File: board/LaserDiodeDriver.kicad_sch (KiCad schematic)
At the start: 54 parts, among them K1 G5V-2_Split, Q1 2N7002, Q2 IRF9Z34, SW1 SW_SPDT, U1 LM317_TO-220, U2 OPA4192, U3 LT1009

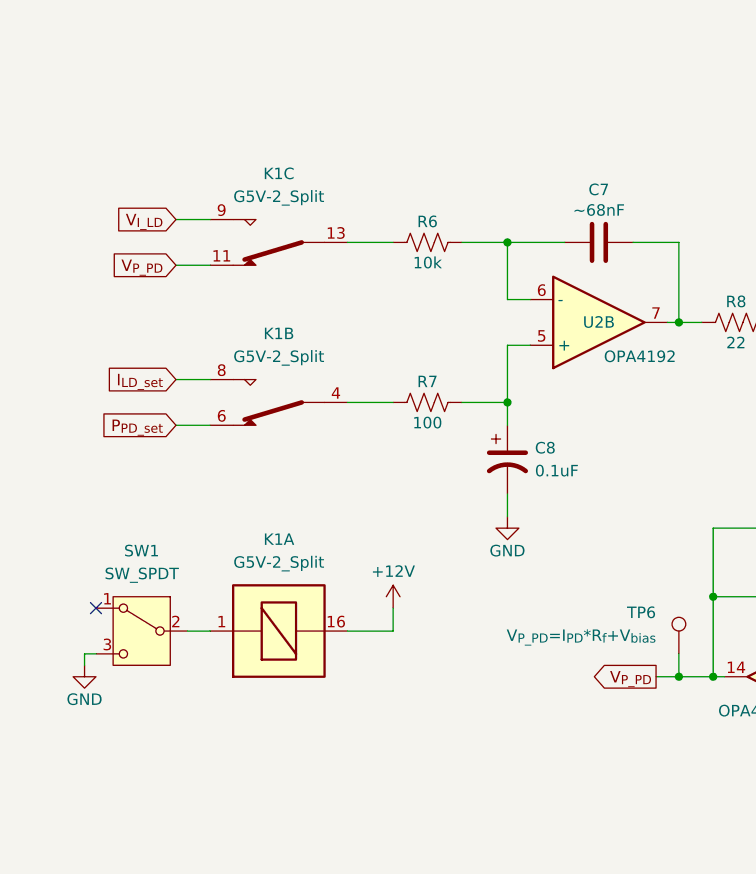
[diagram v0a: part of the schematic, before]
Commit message: Swapped to different signal relay
Since the signal relay is so large relative to all other components, It may be better to find an alternative. Something quicker than 0 Ohm jumpers but smaller than a telecoms signal relay that still preserves good signal integrity with good contacts.
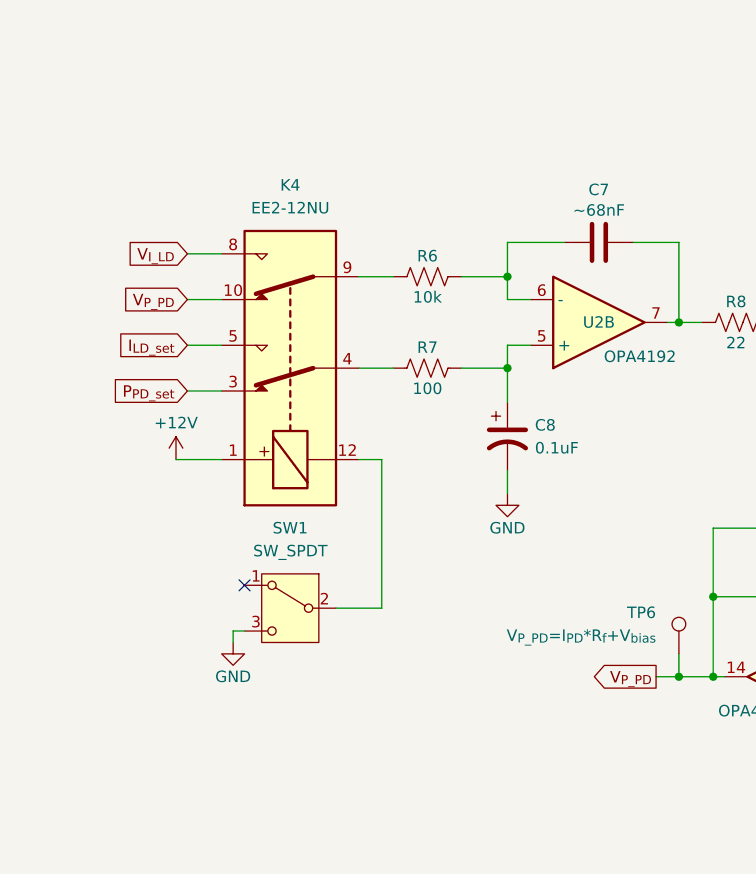
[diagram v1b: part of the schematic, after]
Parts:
- removed K1: G5V-2_Split, Relay_THT:Relay_DPDT_Omron_G5V-2, symbol Relay:G5V-2_Split
- added K4: EE2-12NU, Relay_SMD:Relay_DPDT_Kemet_EE2_NU, symbol Relay:EE2-12NU
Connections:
- net +12V: now also K4.1
- net I_{LD_set}: now also K4.5
- net P_{PD_set}: now also K4.3
- net V_{I_LD}: now also K4.8
- net V_{P_PD}: now also K4.10
- net at R7.1: now also K4.4
- net at SW1.2 (B): now also K4.12
- net at R6.1: now also K4.9
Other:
- moved on the sheet: C8, R6, R7, SW1

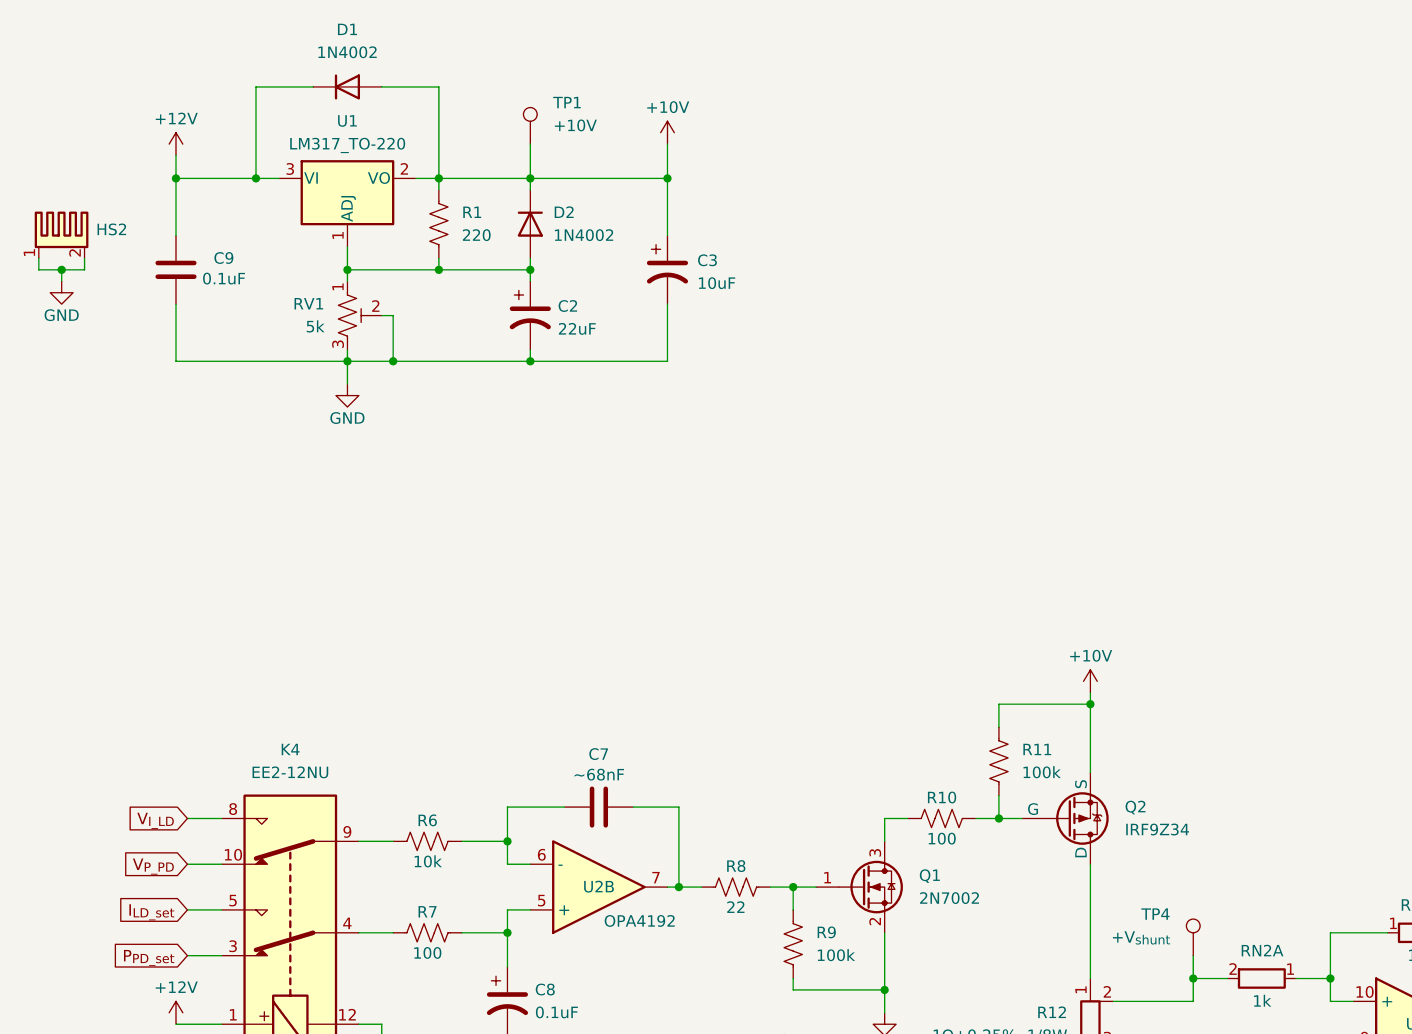
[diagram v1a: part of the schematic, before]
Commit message: Added heatsink for P-FET and LM317, slide switch, and power connector
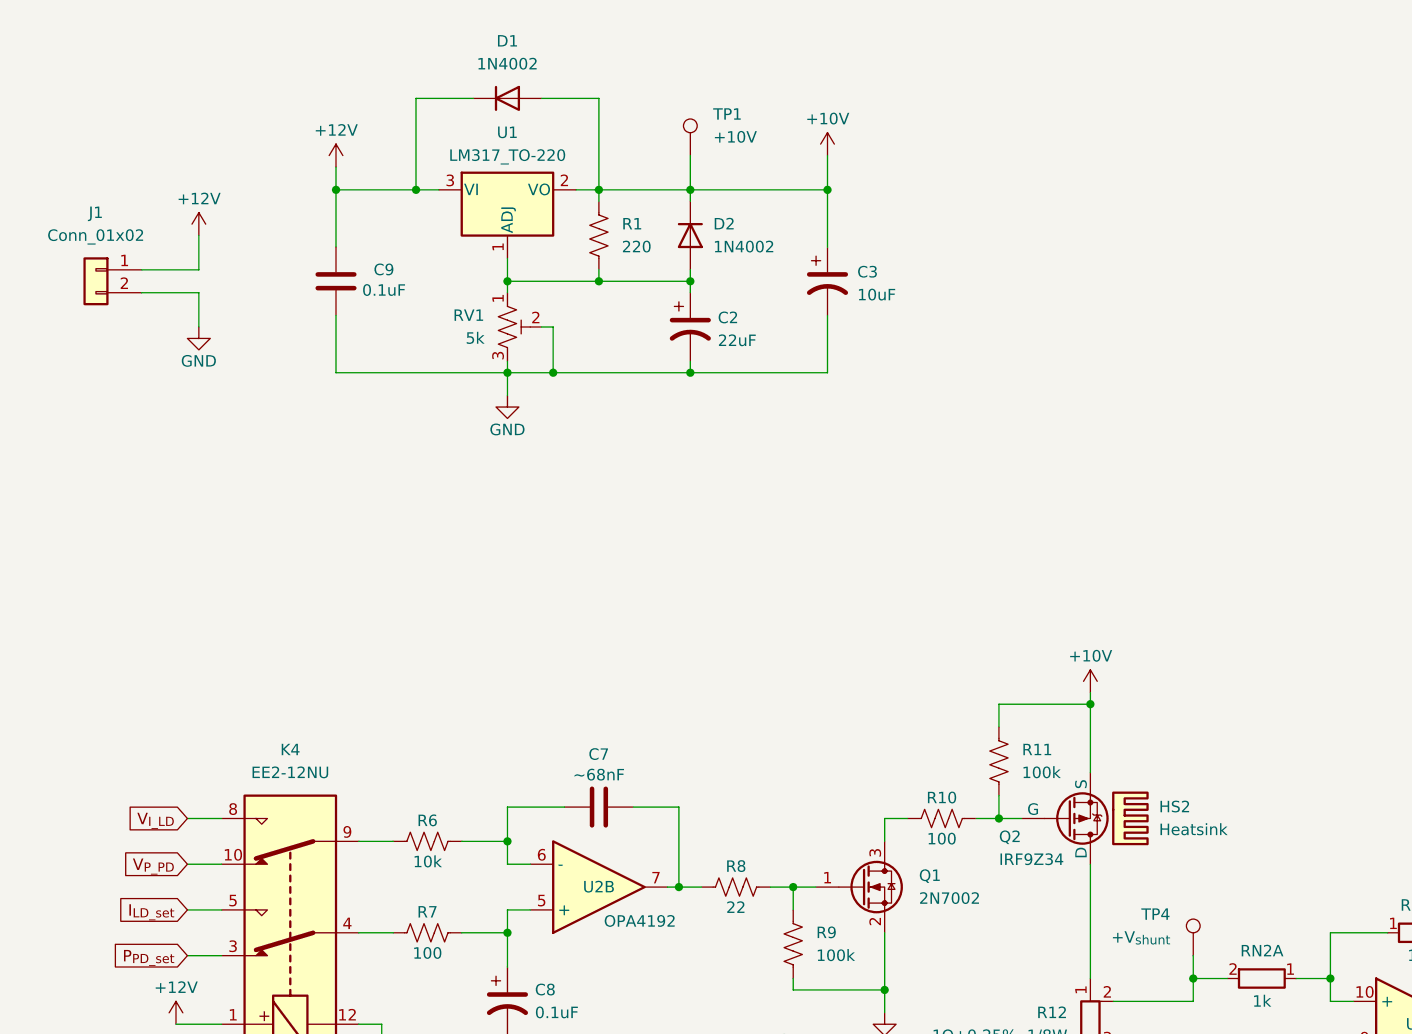
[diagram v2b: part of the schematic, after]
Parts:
- removed HS2: Heatsink_Pad_2Pin, Heatsink:Heatsink_AAVID_Extruded_531002B00000G_34.9x12.7mm_H25.4mm, symbol Mechanical:Heatsink_Pad_2Pin
- added HS2: Heatsink, Heatsink:Heatsink_AAVID_Extruded_531002B00000G_34.9x12.7mm_H25.4mm, symbol Mechanical:Heatsink
- added J1: Conn_01x02, Connector_Hirose:Hirose_DF13-02P-1.25DS_1x02_P1.25mm_Horizontal, symbol Connector_Generic:Conn_01x02
- SW1: footprint (none) -> Button_Switch_THT:SW_Slide_SPDT_Straight_CK_OS102011MS2Q; Price $1.22000 -> (none)
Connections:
- net +12V: now also J1.1 (Pin_1)
- net GND: now also J1.2 (Pin_2)
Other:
- moved on the sheet: C2, C3, C9, D1, D2, R1, RV1, TP1, U1

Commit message: Found rectifier diode and ensured things fit to begin layout
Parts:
- removed D1, D2: 1N4002, Diode_THT:D_DO-41_SOD81_P10.16mm_Horizontal, symbol Diode:1N4002
- added D1, D2: US2AA, Diode_SMD:D_SMA, symbol Diode:US2AA
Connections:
- net +10V: now also D1.1 (K), D2.2 (A)
- net +12V: now also D2.1 (K)
- net at C2.1, R1.2, RV1.1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: now also D1.2 (A)
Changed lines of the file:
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@@
 	)
 	(symbol
-		(lib_id "Diode:1N4002")
-		(at 69.85 27.94 0)
-		(unit 1)
-		(exclude_from_sim no)
-		(in_bom yes)
-		(on_board yes)
-		(dnp no)
-		(fields_autoplaced yes)
-		(property "Reference" "D1"
-			(at 69.85 21.59 0)
-			(effects
-				(font
-					(size 1.27 1.27)
-				)
-			)
-		)
-		(property "Value" "1N4002"
-			(at 69.85 24.13 0)
-			(effects
-				(font
-					(size 1.27 1.27)
-				)
-			)
-		)
-		(property "Footprint" "Diode_THT:D_DO-41_SOD81_P10.16mm_Horizontal"
-			(at 69.85 32.385 0)
-			(effects
-				(font
-					(size 1.27 1.27)
-				)
-				(hide yes)
-			)
-		)
-		(property "Datasheet" "http://www.vishay.com/docs/88503/1n4001.pdf"
-			(at 69.85 27.94 0)
-			(effects
-				(font
-					(size 1.27 1.27)
-				)
-				(hide yes)
-			)
-		)
-		(property "Description" "100V 1A General Purpose Rectifier Diode, DO-41"
-			(at 69.85 27.94 0)
-			(effects
-				(font
-					(size 1.27 1.27)
-				)
-				(hide yes)
-			)
-		)
-		(property "Sim.Device" "D"
-			(at 69.85 27.94 0)
-			(effects
-				(font
-					(size 1.27 1.27)
-				)
-				(hide yes)
-			)
-		)
-		(property "Sim.Pins" "1=K 2=A"
-			(at 69.85 27.94 0)
-			(effects
-				(font
-					(size 1.27 1.27)
-				)
-				(hide yes)
-			)
-		)
-		(pin "2"
-		)
-		(pin "1"
-		)
-		(instances
-			(project ""
-				(path "/331385f6-e980-45c6-bdf7-9362279e36d1"
-					(reference "D1")
-					(unit 1)
-				)
-			)
-		)
-	)
-	(symbol
 		(lib_id "power:GND")
 		(at 111.76 129.54 0)
@@
 	)
 	(symbol
+		(lib_id "Diode:US2AA")
+		(at 69.85 27.94 0)
+		(unit 1)
+		(exclude_from_sim no)
+		(in_bom yes)
+		(on_board yes)
+		(dnp no)
+		(fields_autoplaced yes)
+		(property "Reference" "D2"
+			(at 69.85 21.59 0)
+			(effects
+				(font
+					(size 1.27 1.27)
+				)
+			)
+		)
+		(property "Value" "US2AA"
+			(at 69.85 24.13 0)
+			(effects
+				(font
+					(size 1.27 1.27)
+				)
+			)
+		)
+		(property "Footprint" "Diode_SMD:D_SMA"
+			(at 69.85 32.385 0)
+			(effects
+				(font
+					(size 1.27 1.27)
+				)
+				(hide yes)
+			)
+		)
+		(property "Datasheet" "https://www.digikey.com/en/products/detail/onsemi/US2AA/5844483"
+			(at 69.85 27.94 0)
+			(effects
+				(font
+					(size 1.27 1.27)
+				)
+				(hide yes)
+			)
+		)
+		(property "Description" "50V, 1.5A, General Purpose Rectifier Diode, SMA(DO-214AC)"
+			(at 69.85 27.94 0)
+			(effects
+				(font
+					(size 1.27 1.27)
+				)
+				(hide yes)
+			)
+		)
+		(property "Sim.Device" "D"
+			(at 69.85 27.94 0)
+			(effects
+				(font
+					(size 1.27 1.27)
+				)
+				(hide yes)
+			)
+		)
+		(property "Sim.Pins" "1=K 2=A"
+			(at 69.85 27.94 0)
+			(effects
+				(font
+					(size 1.27 1.27)
+				)
+				(hide yes)
+			)
+		)
+		(pin "1"
+		)
+		(pin "2"
+		)
+		(instances
+			(project ""
+				(path "/331385f6-e980-45c6-bdf7-9362279e36d1"
+					(reference "D2")
+					(unit 1)
+				)
+			)
+		)
+	)
+	(symbol
 		(lib_id "Device:R_Potentiometer_Trim_US")
 		(at 156.21 219.71 0)
@@
 	)
 	(symbol
+		(lib_id "Diode:US2AA")
+		(at 90.17 43.18 270)
+		(unit 1)
+		(exclude_from_sim no)
+		(in_bom yes)
+		(on_board yes)
+		(dnp no)
+		(fields_autoplaced yes)
+		(property "Reference" "D1"
+			(at 92.71 41.9099 90)
+			(effects
+				(font
+					(size 1.27 1.27)
+				)
+				(justify left)
+			)
+		)
+		(property "Value" "US2AA"
+			(at 92.71 44.4499 90)
+			(effects
+				(font
+					(size 1.27 1.27)
+				)
+				(justify left)
+			)
+		)
+		(property "Footprint" "Diode_SMD:D_SMA"
+			(at 85.725 43.18 0)
+			(effects
+				(font
+					(size 1.27 1.27)
+				)
+				(hide yes)
+			)
+		)
+		(property "Datasheet" "https://www.digikey.com/en/products/detail/onsemi/US2AA/5844483"
+			(at 90.17 43.18 0)
+			(effects
+				(font
+					(size 1.27 1.27)
+				)
+				(hide yes)
+			)
+		)
+		(property "Description" "50V, 1.5A, General Purpose Rectifier Diode, SMA(DO-214AC)"
+			(at 90.17 43.18 0)
+			(effects
+				(font
+					(size 1.27 1.27)
+				)
+				(hide yes)
+			)
+		)
+		(property "Sim.Device" "D"
+			(at 90.17 43.18 0)
+			(effects
+				(font
+					(size 1.27 1.27)
+				)
+				(hide yes)
+			)
+		)
+		(property "Sim.Pins" "1=K 2=A"
+			(at 90.17 43.18 0)
+			(effects
+				(font
+					(size 1.27 1.27)
+				)
+				(hide yes)
+			)
+		)
+		(pin "1"
+		)
+		(pin "2"
+		)
+		(instances
+			(project "LaserDiodeDriver"
+				(path "/331385f6-e980-45c6-bdf7-9362279e36d1"
+					(reference "D1")
+					(unit 1)
+				)
+			)
+		)
+	)
+	(symbol
 		(lib_id "power:GND")
 		(at 176.53 224.79 0)
@@
 					(unit 1)
 				)
-			)
-		)
-	)
-	(symbol
-		(lib_id "Diode:1N4002")
-		(at 90.17 43.18 270)
-		(unit 1)
-		(exclude_from_sim no)
-		(in_bom yes)
-		(on_board yes)
-		(dnp no)
-		(fields_autoplaced yes)
-		(property "Reference" "D2"
-			(at 92.71 41.9099 90)
-			(effects
-				(font
-					(size 1.27 1.27)
-				)
-				(justify left)
-			)
-		)
-		(property "Value" "1N4002"
-			(at 92.71 44.4499 90)
-			(effects
-				(font
-					(size 1.27 1.27)
-				)
-				(justify left)
-			)
-		)
-		(property "Footprint" "Diode_THT:D_DO-41_SOD81_P10.16mm_Horizontal"
-			(at 85.725 43.18 0)
-			(effects
-				(font
-					(size 1.27 1.27)
-				)
-				(hide yes)
-			)
-		)
-		(property "Datasheet" "http://www.vishay.com/docs/88503/1n4001.pdf"
-			(at 90.17 43.18 0)
-			(effects
-				(font
-					(size 1.27 1.27)
-				)
-				(hide yes)
-			)
-		)
-		(property "Description" "100V 1A General Purpose Rectifier Diode, DO-41"
-			(at 90.17 43.18 0)
-			(effects
-				(font
-					(size 1.27 1.27)
-				)
-				(hide yes)
-			)
-		)
-		(property "Sim.Device" "D"
-			(at 90.17 43.18 0)
-			(effects
-				(font
-					(size 1.27 1.27)
-				)
-				(hide yes)
-			)
-		)
-		(property "Sim.Pins" "1=K 2=A"
-			(at 90.17 43.18 0)
-			(effects
-				(font
-					(size 1.27 1.27)
-				)
-				(hide yes)
-			)
-		)
-		(pin "2"
-		)
-		(pin "1"
-		)
-		(instances
-			(project "LaserDiodeDriver"
-				(path "/331385f6-e980-45c6-bdf7-9362279e36d1"
-					(reference "D2")
-					(unit 1)
-				)
